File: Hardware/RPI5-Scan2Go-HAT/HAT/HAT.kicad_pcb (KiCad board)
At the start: 2 copper layers, 76 x 96.5 mm, 39 parts, among them J1 RPi_GPIO, J10 Conn_01x02_Socket, J12 Conn_01x02_Socket, J13 Conn_01x02_Socket, J14 Conn_01x02_Socket, J15 Jack-DC 5V, J18 Conn_01x02_Socket, J19 Conn_01x02_Socket, J2 Conn_01x04_Socket, J20 Conn_01x05_Socket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

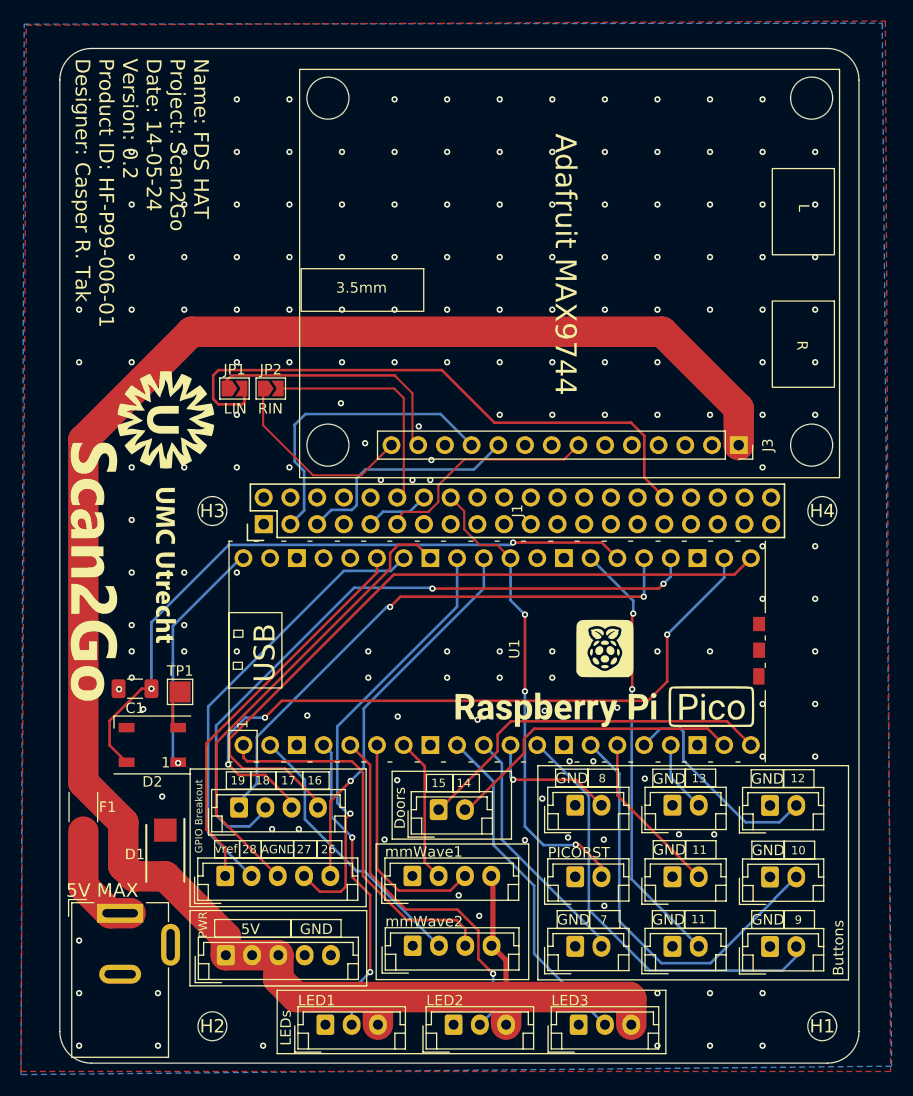
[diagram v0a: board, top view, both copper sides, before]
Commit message: Updated PCB to v0.2.1, improved docs
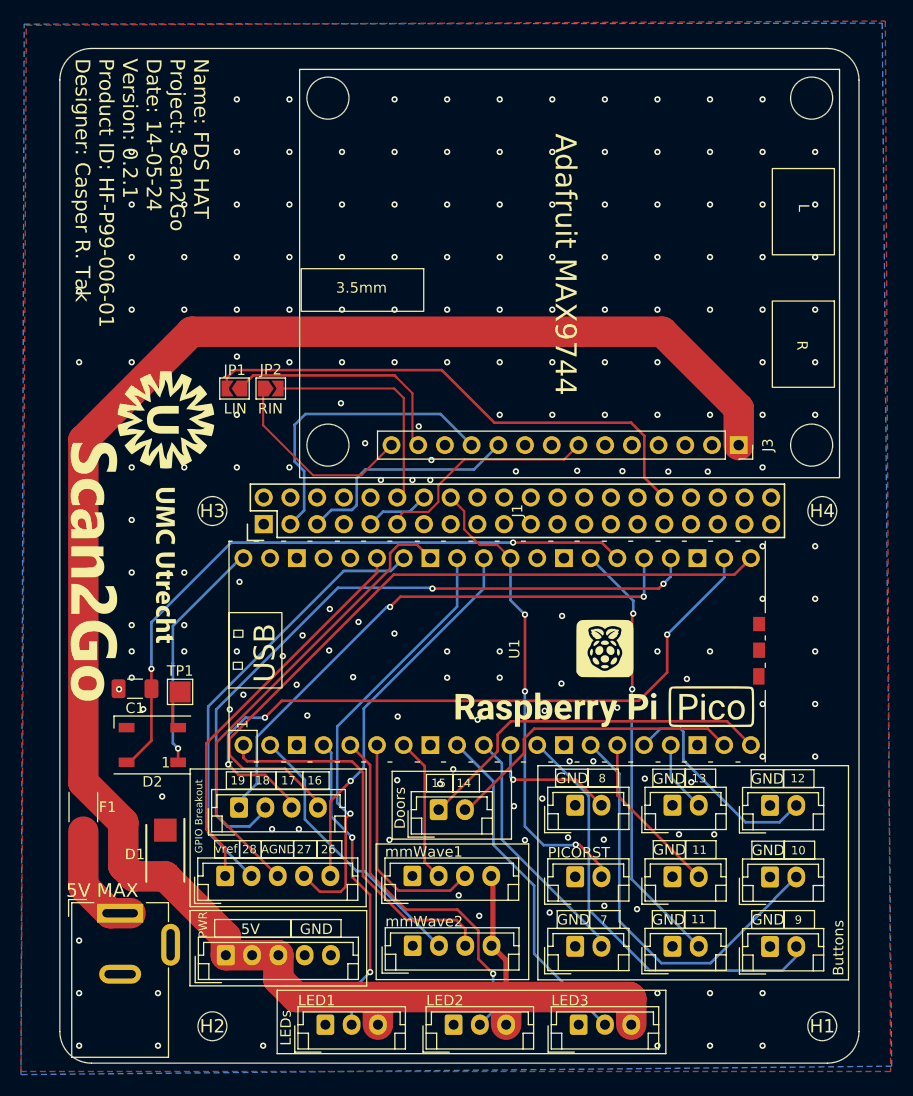
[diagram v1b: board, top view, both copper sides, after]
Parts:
- turned JP1 to 180 degrees
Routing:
- net Net-(J1-BCM12_PWM0): track 57.2 -> 50.3 mm
- net Net-(J3-LIN): track 25.1 -> 22.9 mm
- net Net-(D2-DIN): track 64.2 -> 62.5 mm
- net Net-(J2-Pin_2): track 66.1 -> 67.0 mm
- net Net-(J2-Pin_3): track 68.1 -> 67.6 mm
- net GND: vias 165 -> 185
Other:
- board text added: "Name: FDS HAT Project: Scan2Go Date: 14-05-24 Version: 0.2.1 Product ID: HF-P99-006-01 Designer: Casper R. Tak"
- board text removed: "Name: FDS HAT Project: Scan2Go Date: 14-05-24 Version: 0.2 Product ID: HF-P99-006-01 Designer: Casper R. Tak"

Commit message: Improved bom file and cleanup
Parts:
- F1: value 10 A -> 5 A
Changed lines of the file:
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@@
 			)
 		)
-		(property "Value" "10 A"
+		(property "Value" "5 A"
 			(at 0 2.28 -90)
 			(layer "F.Fab")

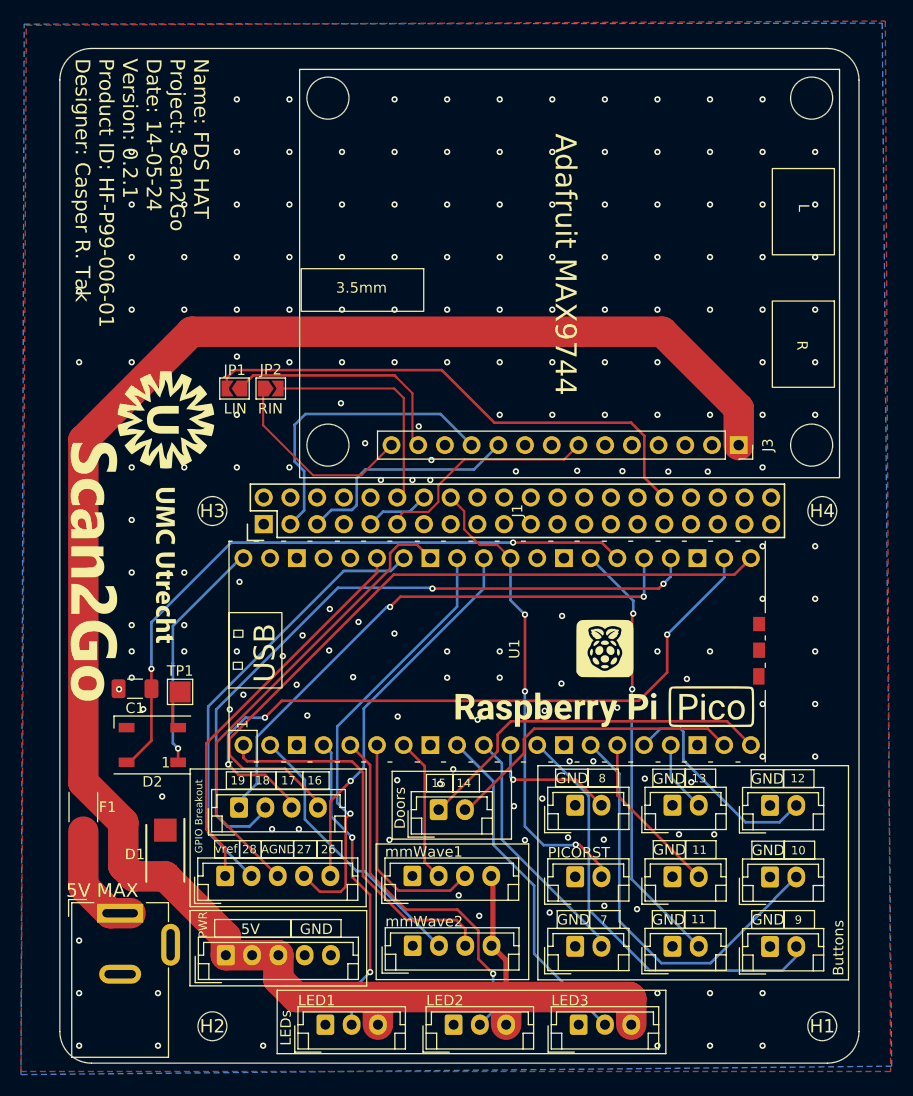
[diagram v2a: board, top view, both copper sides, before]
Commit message: added V0.3 of pcb (srlatch) and added librarys
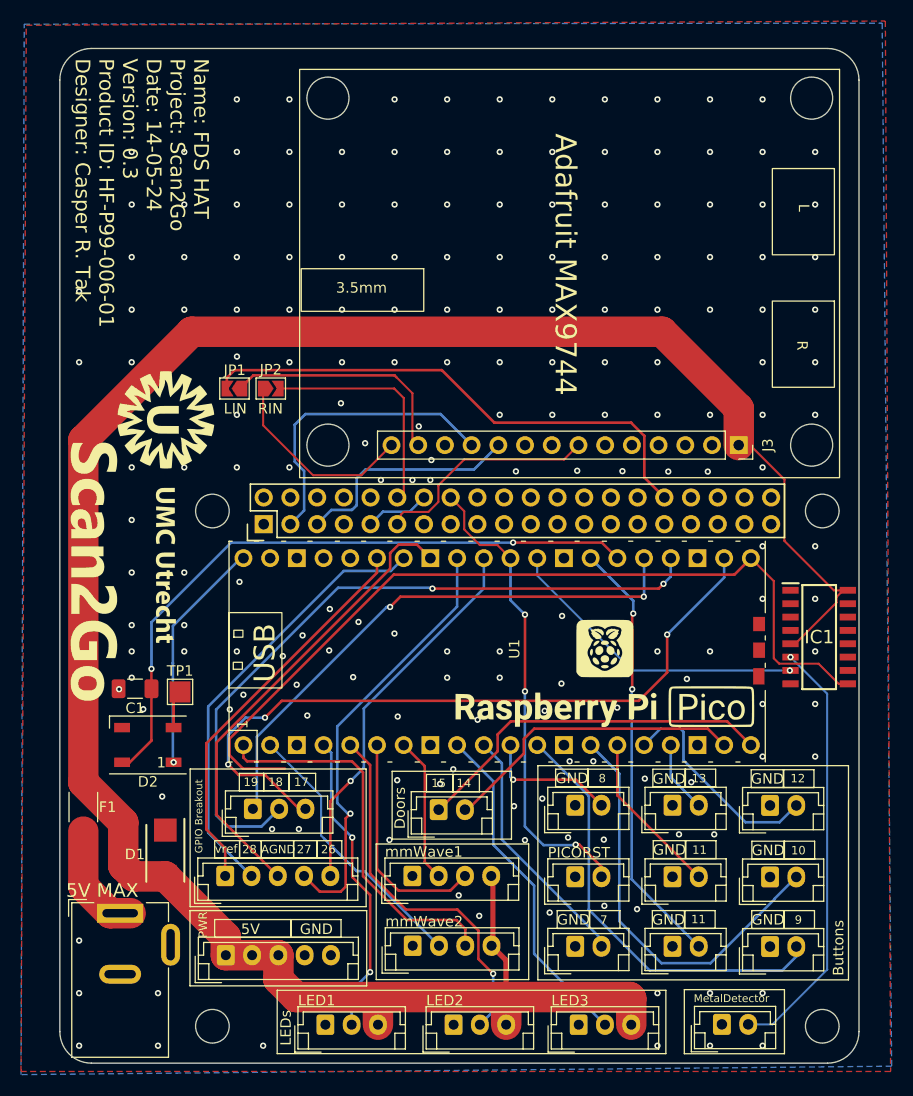
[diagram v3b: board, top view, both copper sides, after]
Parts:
- removed J2: Conn_01x04_Socket, Connector_JST:JST_EH_B4B-EH-A_1x04_P2.50mm_Vertical
- added IC1: MC14043BDR2G, SamacSys_Parts:SOIC127P600X175-16N, F.Cu at (135.4, 96.1)
- added J11: Conn_01x02_Socket, Connector_JST:JST_EH_B2B-EH-A_1x02_P2.50mm_Vertical, F.Cu at (126.1, 133.0)
- added J16: Conn_01x03_Socket, Connector_JST:JST_EH_B3B-EH-A_1x03_P2.50mm_Vertical, F.Cu at (81.5, 112.5)
- D1: value SMBJ26A -> 5.0V
- H1, H2, H3, H4: footprint (none) -> MountingHole:MountingHole_3.2mm_M3
- moved D2 0.43 mm to (71.5, 106.4)
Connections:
- U1 pad 21: Net-(J2-Pin_4) -> /Latch-out
- U1 pad 29: unconnected-(U1-GPIO22-Pad29) -> /Latch-RST
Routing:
- net /Latch-out: track 0.00 -> 82.6 mm
- net Net-(J2-Pin_4): track 68.5 -> 0.00 mm
- net Net-(IC1-S1): track 0.00 -> 40.8 mm, vias 0 -> 1
- net /Latch-RST: track 0.00 -> 29.5 mm, vias 0 -> 1
- net +5V: track 190.9 -> 218.3 mm
- net Net-(J16-Pin_3): track 67.6 -> 69.2 mm
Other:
- board text added: "MetalDetector"
- board text added: "Name: FDS HAT Project: Scan2Go Date: 14-05-24 Version: 0.3 Product ID: HF-P99-006-01 Designer: Casper R. Tak"
- board text removed: "16"
- board text removed: "Name: FDS HAT Project: Scan2Go Date: 14-05-24 Version: 0.2.1 Product ID: HF-P99-006-01 Designer: Casper R. Tak"

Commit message: added v0.3.1
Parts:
- added R1: 10K, Resistor_SMD:R_1206_3216Metric_Pad1.30x1.75mm_HandSolder, F.Cu at (134.4, 89.3)
- moved IC1 0.19 mm to (135.2, 96.1)
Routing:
- net /Latch-out: track 82.6 -> 18.6 mm
- net Net-(IC1-S1): track 40.8 -> 51.3 mm
- net +5V: track 218.3 -> 217.7 mm
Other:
- board text added: "Name: FDS HAT Project: Scan2Go Date: 21-05-24 Version: 0.3.1 Product ID: HF-P99-006-01 Designer: Casper R. Tak"
- board text removed: "Name: FDS HAT Project: Scan2Go Date: 14-05-24 Version: 0.3 Product ID: HF-P99-006-01 Designer: Casper R. Tak"
